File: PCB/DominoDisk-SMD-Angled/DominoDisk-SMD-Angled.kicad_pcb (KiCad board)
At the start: 4 copper layers, 45 x 35.2 mm, 29 parts, among them J1 Daisy port out, J2 ICSP_ISP6, J3 Daisy port in, J4 UART, K1 TF-104 MicroSD card holder, U1 PC817C-S, U2 ATmega328P-AU, U3 TXB0104PWR level shifter, U4 SE5218ALG voltage regulator, Y1 CSTNE16M0V530000R0 Resonator

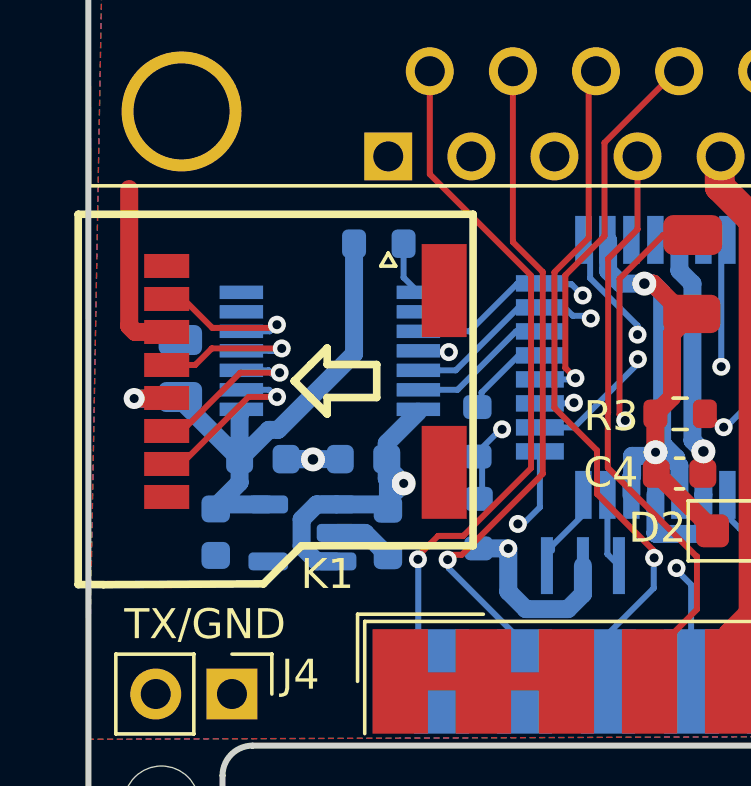
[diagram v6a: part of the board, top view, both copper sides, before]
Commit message: Fix details on DD/angled
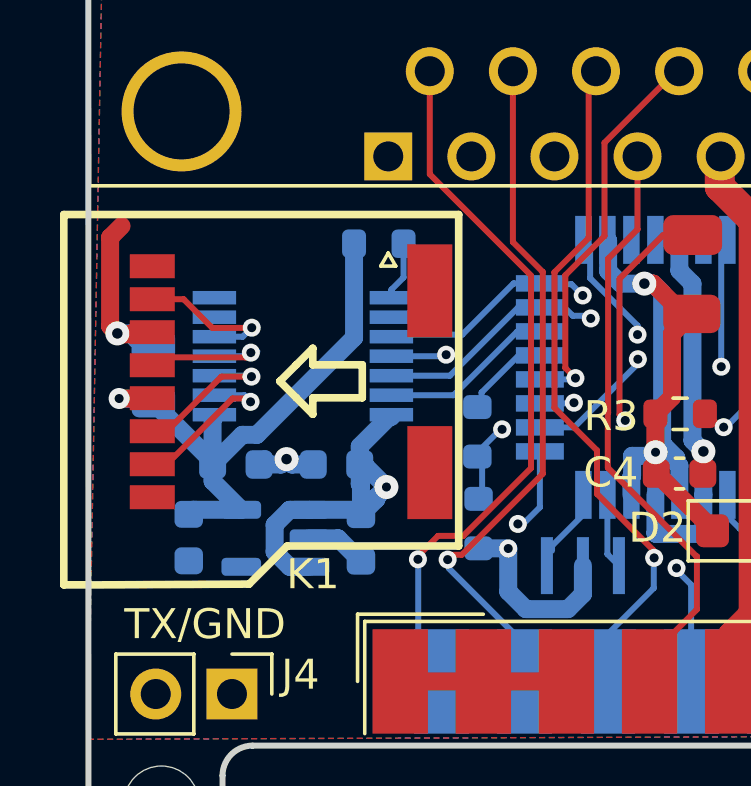
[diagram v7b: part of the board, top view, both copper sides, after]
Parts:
- moved C2 0.92 mm to (107.7, 57.7)
- moved C6 0.92 mm to (102.8, 60.1)
- moved U4 0.92 mm to (105.7, 60.1)
- moved C1 0.92 mm to (101.6, 54.7)
- moved C3 0.92 mm to (104.3, 57.7)
- moved C5 0.92 mm to (108.5, 60.1)
- moved U3 0.92 mm to (106.6, 54.1)
- moved K1 0.48 mm to (106.2, 54.9)
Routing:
- net SCK: track 25.2 -> 26.3 mm
- net 5V_burgerDisk: track 59.9 -> 61.0 mm
- net MISO: track 21.9 -> 22.9 mm
- net MOSI: track 25.3 -> 26.3 mm
- net CS: track 4.86 -> 5.83 mm
- net 3V3: track 19.5 -> 20.1 mm
- net GND: track 41.2 -> 41.3 mm, vias 8 -> 9

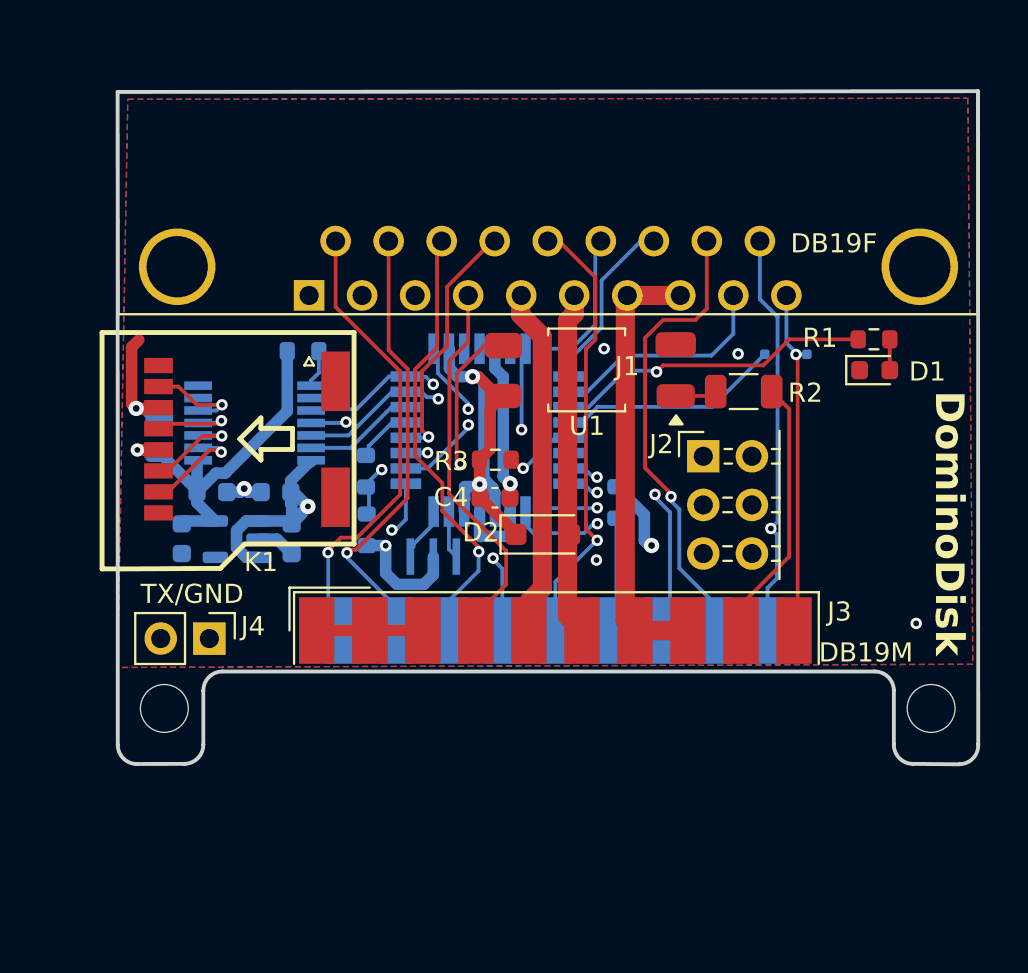
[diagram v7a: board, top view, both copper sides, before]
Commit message: Rework for DB19F on the back
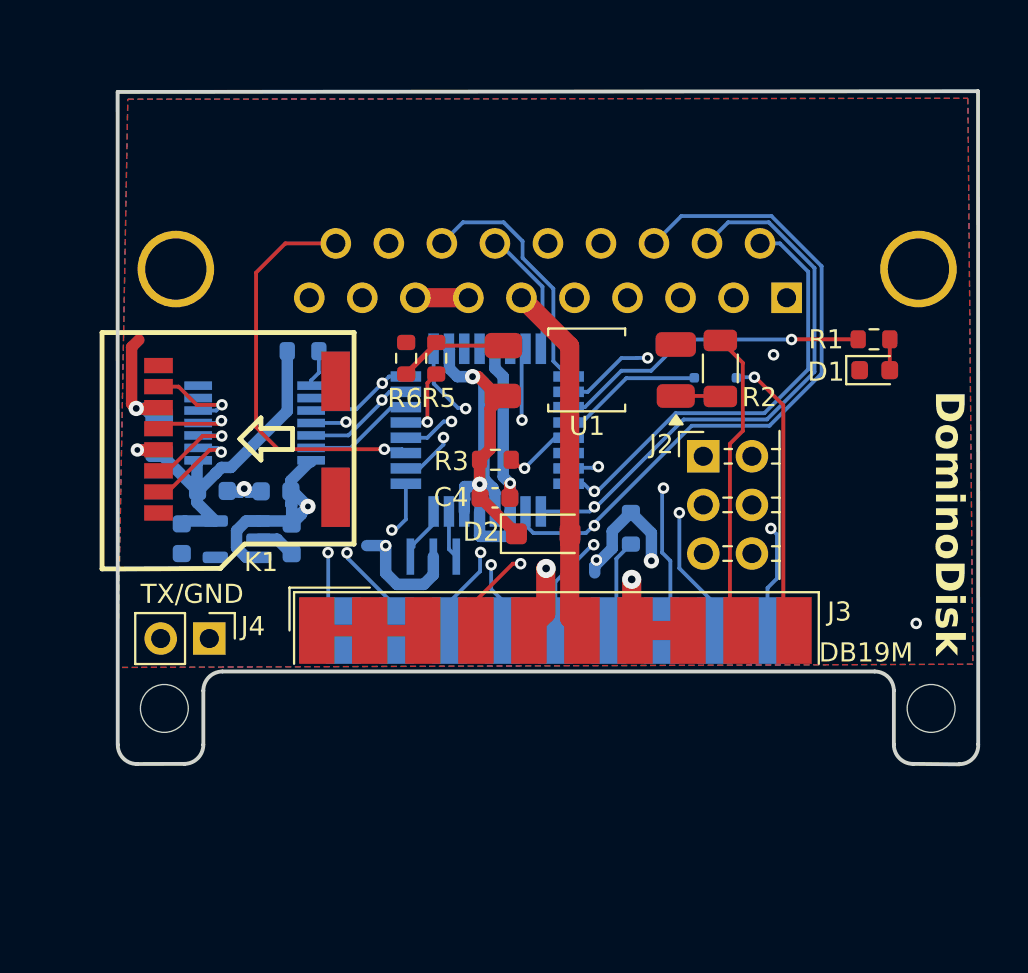
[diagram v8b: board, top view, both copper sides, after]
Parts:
- J1: moved to B.Cu
- R5, R6: moved to F.Cu
- moved J1 24.9 mm to (134.4, 47.5), turned to 0 degrees
- moved R6 9.19 mm to (114.5, 50.7), turned to -90 degrees
- moved R5 6.95 mm to (116.1, 50.7), turned to 90 degrees
- moved D3 3.88 mm to (130.6, 51.7)
- moved R2 1.72 mm to (130.9, 51.2), turned to -90 degrees
- moved R7 1.55 mm to (126.2, 59.6)
- moved C3 0.07 mm to (104.4, 57.6)
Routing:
- net WRPROT_out: track 18.3 -> 41.3 mm
- net +12V: track 23.3 -> 44.3 mm, vias 0 -> 1
- net PH2: track 33.4 -> 47.3 mm
- net DRV2_out: track 11.9 -> 21.1 mm, vias 0 -> 1
- net PH1: track 39.1 -> 48.0 mm
- net WRDATA: track 41.9 -> 49.0 mm
- net Net-(R5-Pad2): track 14.3 -> 8.00 mm, vias 2 -> 0
- net PH3_out: track 13.2 -> 18.9 mm
- net RDDATA: track 39.7 -> 34.0 mm
- net WREQ: track 23.1 -> 28.7 mm
- net EN3.5: track 18.9 -> 24.3 mm, vias 0 -> 1
- net WRPROT_in: track 11.7 -> 7.53 mm
- net DRV1_out: track 9.31 -> 13.1 mm
- net DRV2_in: track 12.6 -> 16.2 mm
- net GND: track 41.3 -> 44.2 mm, vias 9 -> 8
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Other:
- board text added: "SOLDER FEMALE DB19 ON THIS SIDE"
